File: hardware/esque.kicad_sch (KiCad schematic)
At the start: 11 parts, among them J2 Conn_01x03_Pin, J3 Conn_01x04_Pin

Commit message: Update two-board hardware design to revision 0.9
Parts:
- removed A1: Arduino_Nano_v2.x, Module:Arduino_Nano, symbol MCU_Module:Arduino_Nano_v2.x
- removed D1, D2: LED, LED_THT:LED_D3.0mm_Horizontal_O6.35mm_Z10.0mm, symbol Device:LED
- removed J2: Conn_01x03_Pin, Connector_PinHeader_2.54mm:PinHeader_1x03_P2.54mm_Vertical, symbol Connector:Conn_01x03_Pin
- removed J3: Conn_01x04_Pin, Connector:FanPinHeader_1x04_P2.54mm_Vertical, symbol Connector:Conn_01x04_Pin
- added C1, C2: 10pF, Capacitor_SMD:C_1206_3216Metric, symbol Device:C
- added C3, C4: 100nF, Capacitor_SMD:C_1206_3216Metric, symbol Device:C
- added C6: 10uF 16V, Turbimeter:CP_Radial_D5_P2_SingleFace, symbol Device:C_Polarized
- added D1: BPW34 scatter, Turbimeter:BPW34_Holder_v08, symbol Sensor_Optical:BPW34
- added D2: BPW34 reference, Turbimeter:BPW34_Holder_v08, symbol Sensor_Optical:BPW34
- added J1: SENSOR_LINK_2mm, Turbimeter:StackHeader_1x06_P2mm_Base_SingleFace, symbol Connector_Generic:Conn_01x06
- added J2: USB2_CABLE_4_WIRES, Turbimeter:USB_Cable_WireHoles_2x02_P2mm, symbol Connector_Generic:Conn_01x04
- added J4: USB_STACK_4_1.27mm, Turbimeter:USB_StackHeader_2x02_P1.27mm_Base_v09, symbol Connector_Generic:Conn_02x02_Odd_Even
- added R4: 10k, Resistor_SMD:R_1206_3216Metric, symbol Device:R
- added U1: MCP6002-E/P, Turbimeter:MCP6002_DIP8_SingleFace, symbol Turbimeter:MCP6002_DIP8
- D3: value LED -> 850 nm IR; footprint LED_THT:LED_D3.0mm_Horizontal_O6.35mm_Z10.0mm -> Turbimeter:LED850_LeadPads_P2.54mm
- R1, R2: value R -> 1M; footprint Resistor_THT:R_Axial_DIN0207_L6.3mm_D2.5mm_P10.16mm_Horizontal -> Resistor_SMD:R_1206_3216Metric
- R3: value R -> 10k; footprint Resistor_THT:R_Axial_DIN0207_L6.3mm_D2.5mm_P10.16mm_Horizontal -> Resistor_SMD:R_1206_3216Metric
- R5, R6: value R -> 220R; footprint Resistor_THT:R_Axial_DIN0207_L6.3mm_D2.5mm_P10.16mm_Horizontal -> Resistor_SMD:R_1206_3216Metric
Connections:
- net D3 is gone; now on net GND: D3.1 (K)
- net GND: now also C3.2, C4.2, C6.2, D1.2 (A), D2.2 (A), J1.1 (Pin_1), J1.6 (Pin_6), J2.2 (Pin_2), J4.2 (Pin_2), R4.2, U1.4 (V-)
- net 3V3: now reaches R3.1
- net 3V3: now also C4.1, C6.1, J1.2 (Pin_2), U1.8 (V+)
- net REFERENCE_OUT: now reaches R2.1
- net REFERENCE_OUT: now also C2.1, J1.5 (Pin_5), U1.7
- net LED_ANODE: now reaches D3.2 (A)
- net LED_ANODE: now also R6.2; no longer R1.1
- removed net +3.3V: R1.2, R2.2, R3.2, R5.2, R6.2
- net A4 renamed LED_R1
- net LED_R1: now also R5.2
- net A5 renamed LED_DRIVE
- net LED_DRIVE: now also J1.3 (Pin_3)
- new net REFERENCE_SUM: C2.2, D2.1 (K), R2.2, U1.6 (-)
- new net SCATTER_OUT: C1.1, J1.4 (Pin_4), R1.1, U1.1
- new net SCATTER_SUM: C1.2, D1.1 (K), R1.2, U1.2 (-)
- new net USB_DM: J2.3 (Pin_3), J4.3 (Pin_3)
- new net USB_DP: J2.4 (Pin_4), J4.4 (Pin_4)
- new net USB_VBUS: J2.1 (Pin_1), J4.1 (Pin_1)
- new net VREF: C3.1, R3.2, R4.1, U1.3 (+), U1.5 (+)
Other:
- note added: "C4 near U1 VDD. C6 positive to 3V3."
- note added: "D1 faces the cuvette at 90 deg; D2 sees a fixed LED pick-off, shielded from the sample."
- note added: "D7 through J1; two 220 ohm resistors in series."
- note added: "FLOOR 1 - SENSOR / CABLE ENTRY - TWO-BOARD ASSEMBLY"
- note added: "J1: analog/power link. J4: USB link. Both MALE THT on TOP; solder on BOTTOM."
- note added: "J2: four THT wire holes. 1 VBUS, 2 GND, 3 D-, 4 D+. Phone plug must supply device/OTG CC termination."
- note added: "Keep the proven BASE outline, including the lower-left cable passage. Provide cable strain relief."
- note added: "R1/R2=1M, C1/C2=10pF: starting values; tune each channel and check saturation."
- note added: "R3/R4=10k 1%; VREF ~1.65V is amplifier bias."
- note added: "THT components on TOP. All SMD on BOTTOM. All soldering and tracks on B.Cu only. UNROUTED."
- note removed: "Micro"
- note removed: "led"
- note removed: "pantalla"
- note removed: "sensor"
- title: (none) -> Turbidimeter - sensor

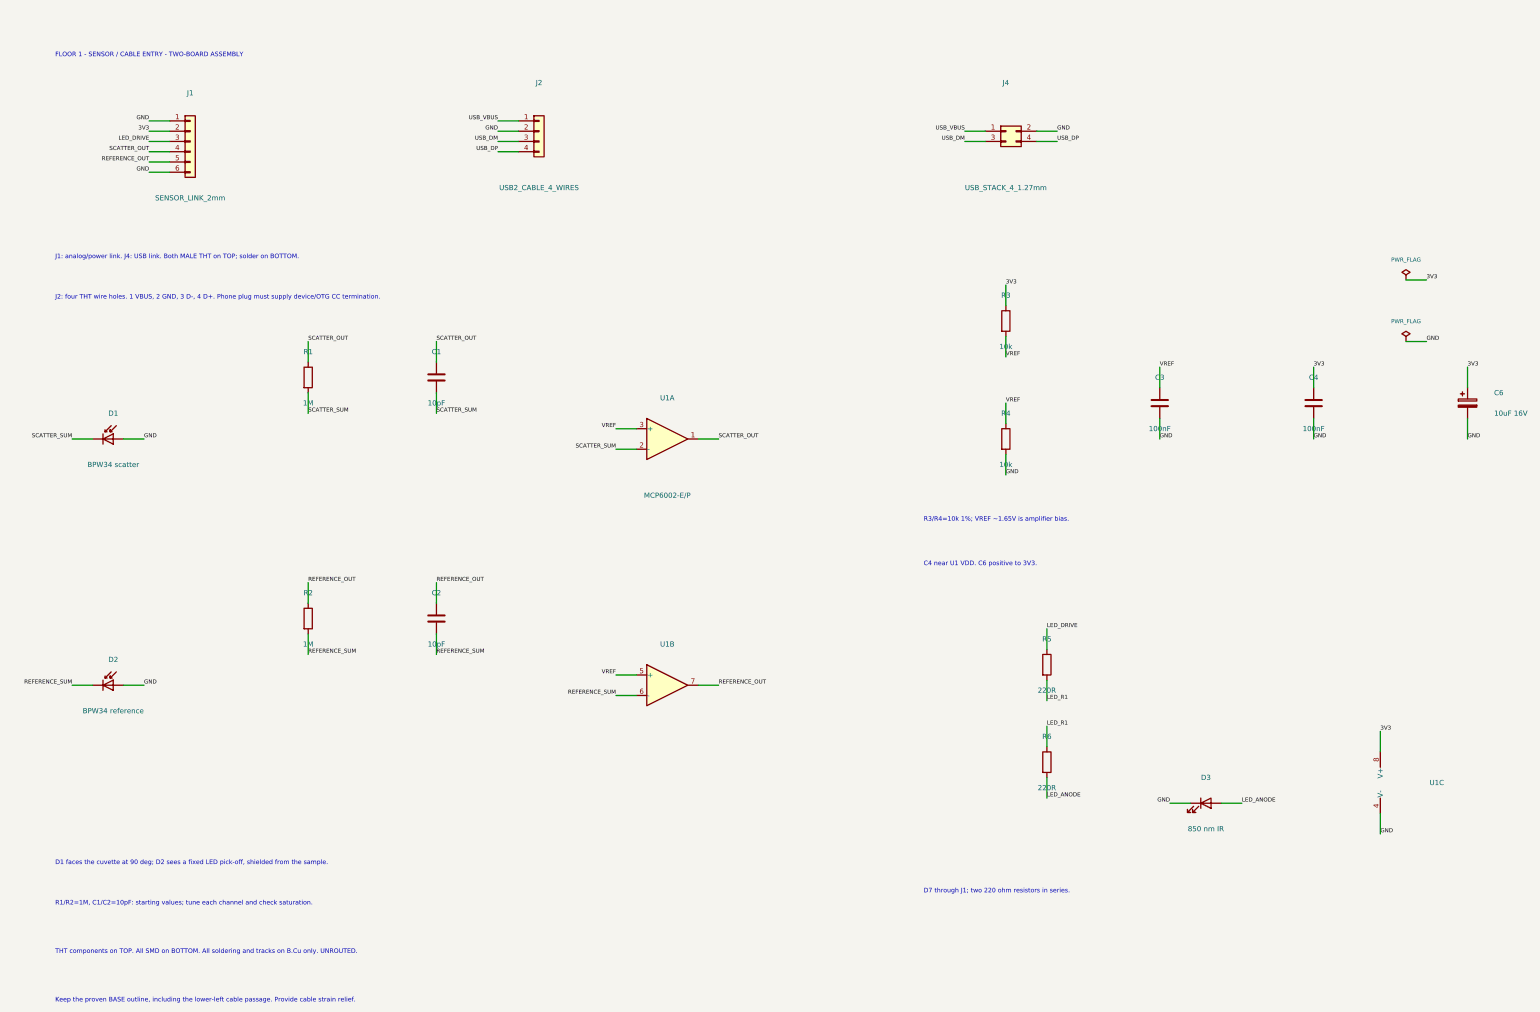
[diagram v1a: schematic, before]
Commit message: Update 32 files (3D, docs, hardware, raíz)
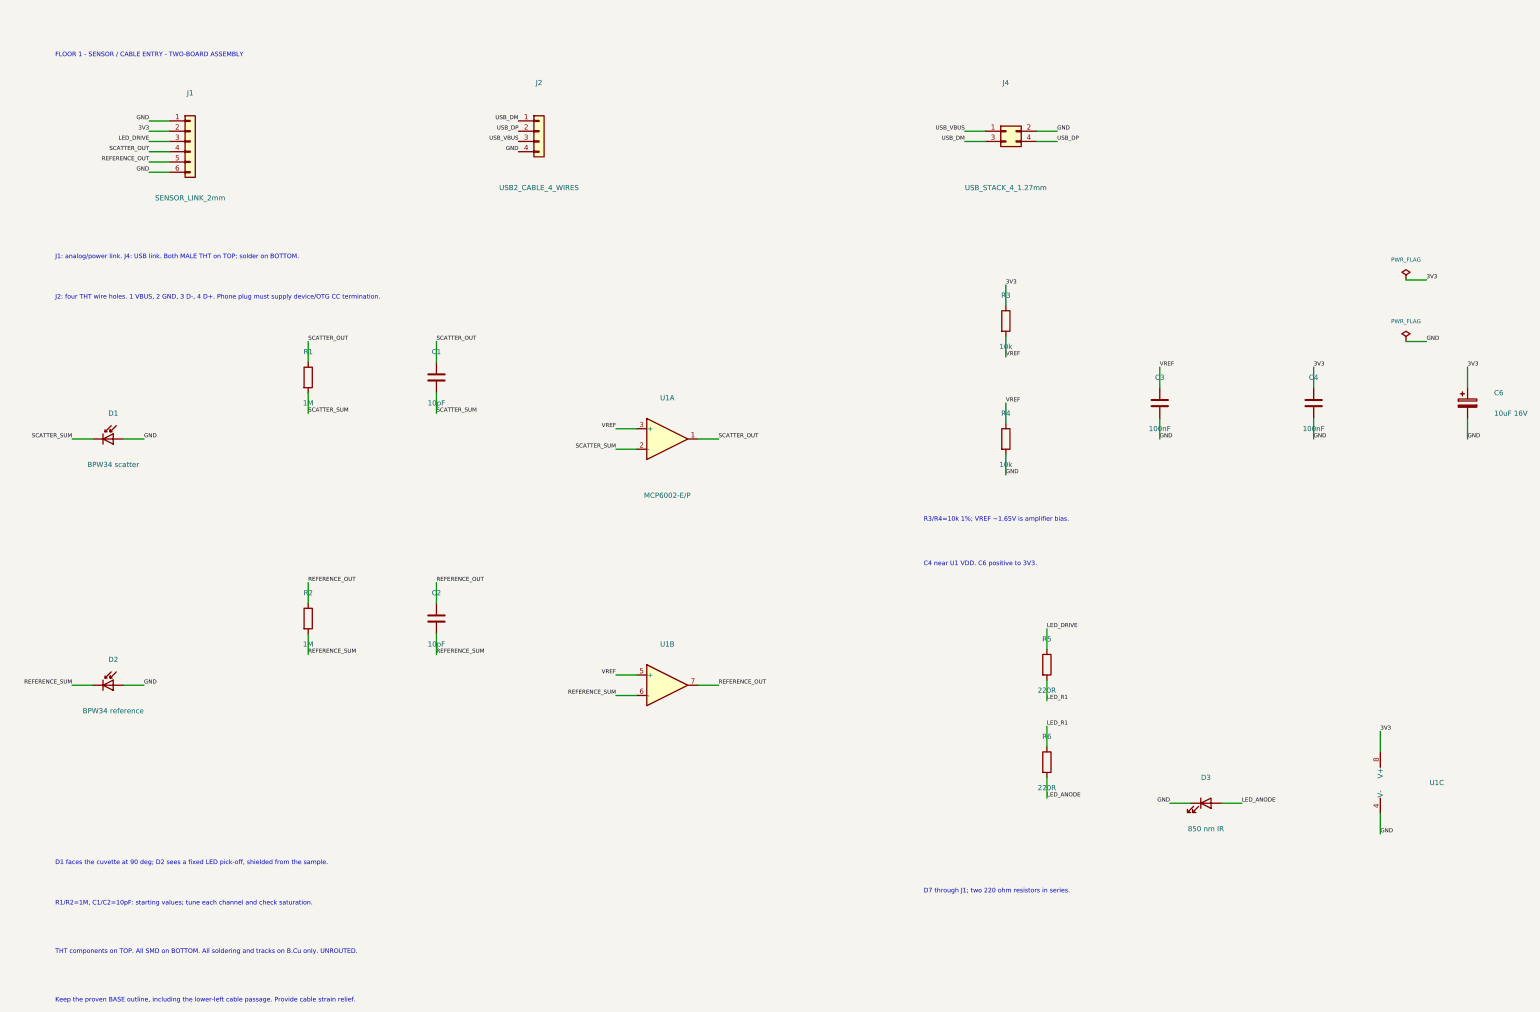
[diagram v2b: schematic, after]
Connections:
- net GND: now also J2.4 (Pin_4); no longer J2.2 (Pin_2)
- net USB_DM: now also J2.1 (Pin_1); no longer J2.3 (Pin_3)
- net USB_DP: now also J2.2 (Pin_2); no longer J2.4 (Pin_4)
- net USB_VBUS: now also J2.3 (Pin_3); no longer J2.1 (Pin_1)

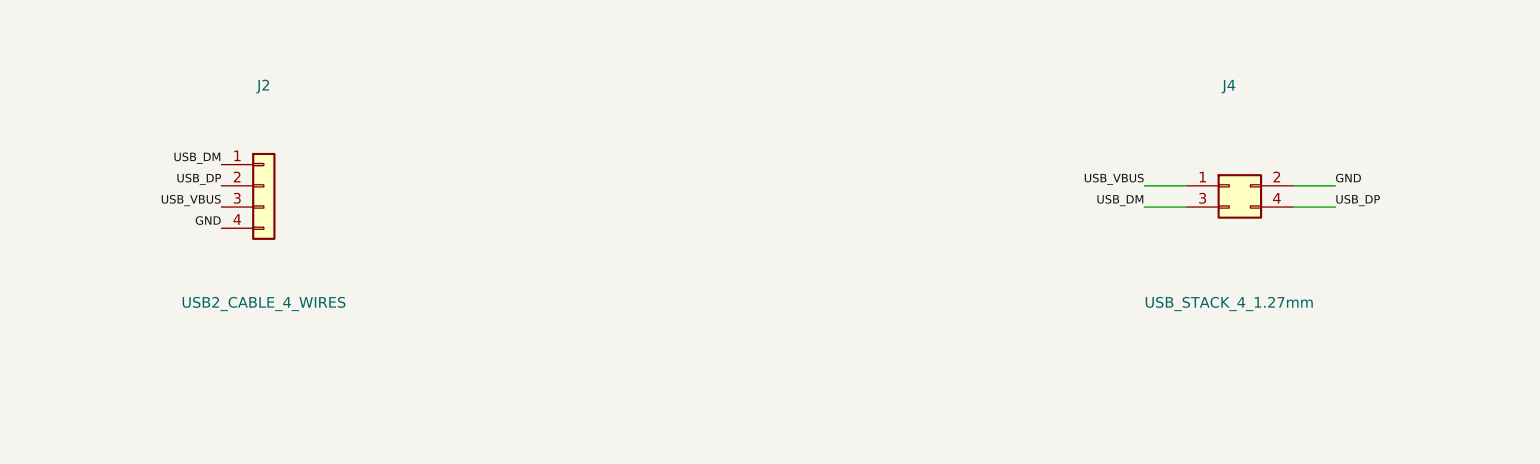
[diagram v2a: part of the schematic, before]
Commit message: Organize project, add calibration app and record prototype bench results
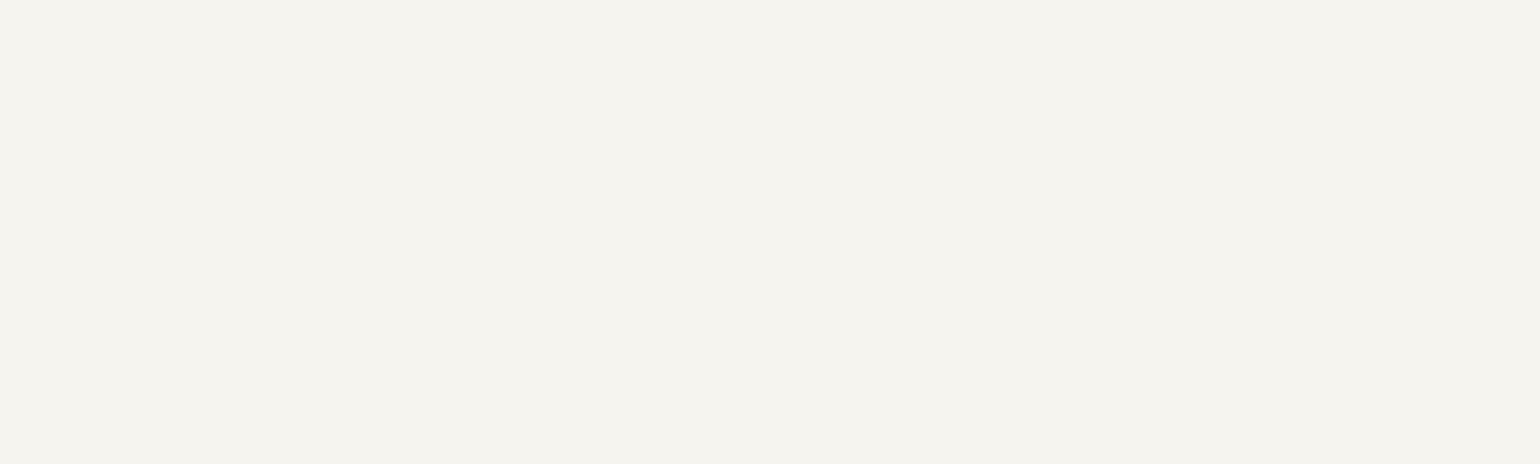
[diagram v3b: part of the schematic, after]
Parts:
- removed J2: USB2_CABLE_4_WIRES, Turbimeter:USB_Cable_WireHoles_2x02_P2mm, symbol Connector_Generic:Conn_01x04
- removed J4: USB_STACK_4_1.27mm, Turbimeter:USB_StackHeader_2x02_P1.27mm_Base_v09, symbol Connector_Generic:Conn_02x02_Odd_Even
- C1, C2, C3, C4: footprint Capacitor_SMD:C_1206_3216Metric -> Capacitor_THT:C_Disc_D5.0mm_W2.5mm_P2.50mm
- J1: footprint Turbimeter:StackHeader_1x06_P2mm_Base_SingleFace -> Connector_PinSocket_2.54mm:PinSocket_1x06_P2.54mm_Vertical
